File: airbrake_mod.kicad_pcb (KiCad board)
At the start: 2 copper layers, 107.9 x 107.9 mm, 78 parts, among them J1 Conn_Coaxial, J2 USB_C_Receptacle_USB2.0_16P, J3 Conn_01x06_Socket, SW4 SW_Push_Shielded, SW5 SW_Push_Shielded, SW6 SW_Push_Shielded, SW7 SW_Push_Shielded, U1 STM32H743VITx, U2 MAX-M8C, U3 TPS54560BDDA, U4 AP7361C-33E, U5 AP7361C-33E, U6 MX25L25645GM2I, U7 DSF105Q9R0HDR

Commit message: Power Supply Speccing, IMU, Eyeballs
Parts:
- added C23: 4.7u, Capacitor_SMD:C_0805_2012Metric, F.Cu at (105.4, 52.4)
- added U8: LSM6DSO32, Package_LGA:LGA-14_3x2.5mm_P0.5mm_LayoutBorder3x4y, F.Cu at (106.0, 55.0)
- C14, C3, C4, C5, C6, C7: value C -> 4.7u
- C15, C16, C20, C21: value C -> 47u
- C17: value C -> 0.1u
- D1, D2: value LED_Filled -> QBLP601-R5-2897
- L1: value L -> 22u
- R10: value R_US -> 18k
- R12: value R_US -> 82k
- R15, R16: value R_US -> 240
- R17, R18, R19, R20: value R_US -> 5k
- R7, R8: value R_US -> 300k
- R9: value R_US -> 62k
- moved BZ1 5.04 mm to (144.8, 91.9), turned to 90 degrees
- moved C7 0.08 mm to (57.0, 72.7)
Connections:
- U1 pad 32: unconnected-(U1-PC4-Pad32) -> ACCEL_CS
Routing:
- net 3V3_Sensors: track 67.4 -> 131.8 mm, vias 0 -> 2
- net 3V3_MCU: track 170.2 -> 183.2 mm
- net Buzzer_H: track 69.9 -> 79.6 mm
- net ACCEL_CS: track 0.00 -> 8.76 mm
- net MODE_3: track 8.68 -> 17.2 mm
- net MODE_2: track 9.47 -> 17.3 mm
- net MODE_1: track 10.0 -> 17.6 mm
- net MODE_0: track 13.2 -> 20.3 mm
- net ACCEL_SDI: track 2.98 -> 9.74 mm
- net ACCEL_SDO: track 3.59 -> 9.97 mm
- net MCU_I2C1_SCL: track 45.6 -> 40.3 mm
- net ACCEL_SCLK: track 3.48 -> 8.35 mm, vias 0 -> 2
- net Buzzer_L: track 68.2 -> 72.9 mm
- net FLASH_SPI_SCLK: track 43.2 -> 45.0 mm
- net -BATT: track 87.9 -> 88.9 mm, vias 72 -> 75

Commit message: Release Candidate 1
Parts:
- removed the G*** at (63.4, 230.4)
- added C24: 4.7u, Capacitor_SMD:C_0805_2012Metric, F.Cu at (146.2, 80.4)
- added C25: 4.7u, Capacitor_SMD:C_0805_2012Metric, F.Cu at (52.0, 105.5)
- added D6: CLV1L-FKB, LED_SMD:LED_Cree-PLCC4_3.2x2.8mm_CCW, F.Cu at (95.3, 48.3)
- added D7: QBLP601-R5-2897, LED_SMD:LED_0603_1608Metric, F.Cu at (117.8, 51.1)
- added D8: QBLP601-R5-2897, LED_SMD:LED_0603_1608Metric, F.Cu at (103.2, 58.3)
- added D9: CLV1L-FKB, LED_SMD:LED_Cree-PLCC4_3.2x2.8mm_CCW, F.Cu at (121.5, 54.0)
- added J4: Conn_01x03_Socket, Connector_Molex:Molex_Micro-Fit_3.0_43650-0315_1x03_P3.00mm_Vertical, F.Cu at (146.2, 91.2)
- added J5: Conn_01x03_Socket, Connector_JST:JST_XH_B3B-XH-A_1x03_P2.50mm_Vertical, F.Cu at (118.3, 146.4)
- added J6: Conn_02x02_Counter_Clockwise, Connector_PinHeader_1.00mm:PinHeader_2x02_P1.00mm_Vertical, F.Cu at (140.8, 83.1)
- added Q1: DMG2302U, Package_TO_SOT_SMD:SOT-23, F.Cu at (138.0, 89.2)
- added Q2: Si2319CDS, Package_TO_SOT_SMD:SOT-23, F.Cu at (141.4, 89.2)
- added Q3: DMG2302U, Package_TO_SOT_SMD:SOT-23, F.Cu at (140.0, 104.9)
- added Q4: Si2319CDS, Package_TO_SOT_SMD:SOT-23, F.Cu at (141.5, 69.8)
- added Q5: Si2319CDS, Package_TO_SOT_SMD:SOT-23, F.Cu at (138.0, 69.8)
- added R23: 43, Resistor_SMD:R_0805_2012Metric, F.Cu at (94.1, 51.8)
- added R24: 43, Resistor_SMD:R_0805_2012Metric, F.Cu at (95.4, 55.2)
- added R25: 110, Resistor_SMD:R_0805_2012Metric, F.Cu at (96.2, 51.8)
- added R26: 240, Resistor_SMD:R_0805_2012Metric, F.Cu at (111.4, 57.0)
- added R27: 240, Resistor_SMD:R_0805_2012Metric, F.Cu at (99.7, 60.2)
- added R29: 110, Resistor_SMD:R_0805_2012Metric, F.Cu at (117.5, 55.3)
- added R30: 43, Resistor_SMD:R_0805_2012Metric, F.Cu at (117.5, 59.1)
- added R31: 43, Resistor_SMD:R_0805_2012Metric, F.Cu at (117.5, 57.2)
- added R32: 56k, Resistor_SMD:R_0805_2012Metric, F.Cu at (137.4, 64.0)
- added R33: 100k, Resistor_SMD:R_0805_2012Metric, F.Cu at (113.5, 62.4)
- added R34: 100k, Resistor_SMD:R_0805_2012Metric, F.Cu at (113.5, 65.8)
- added SW1: SW_Push_Shielded, 0_airbrake_footprints:R-667766, F.Cu at (107.6, 61.4)
- added SW2: SW_Push_Shielded, 0_airbrake_footprints:R-667766, F.Cu at (138.2, 96.2)
- added SW3: SW_Rotary_1x4_MP, 0_airbrake_footprints:S-2051, F.Cu at (54.6, 112.2)
- added SW9: SW_SPDT_321, 0_airbrake_footprints:CL-SB-12A-01T, F.Cu at (147.9, 100.0)
- added U10: BD4860G-TR, Package_TO_SOT_SMD:SOT-23-5, F.Cu at (131.2, 59.2)
- added U9: BME680, Package_LGA:Bosch_LGA-8_3x3mm_P0.8mm_ClockwisePinNumbering, F.Cu at (61.8, 106.3)
- added Y1: Crystal_GND24, Crystal:Crystal_SMD_2016-4Pin_2.0x1.6mm, F.Cu at (110.3, 71.0)
- BZ1: footprint Buzzer_Beeper:Buzzer_TDK_PS1240P02BT_D12.2mm_H6.5mm -> 0_airbrake_footprints:CMT-322-65-SMT-TR
- C1, C2: value C -> 8p
- moved BZ1 17.7 mm to (140.0, 108.9), turned to 180 degrees
- moved D4 17.0 mm to (138.6, 114.4)
- moved R21 14.9 mm to (137.4, 120.5), turned to -90 degrees
- moved R22 11.4 mm to (138.0, 117.6), turned to 0 degrees
- moved D5 3.61 mm to (137.4, 128.6), turned to 90 degrees
- moved C22 0.64 mm to (140.5, 74.2), turned to 180 degrees
- moved C2 0.62 mm to (112.3, 69.0), turned to -45 degrees
- moved C1 0.58 mm to (112.3, 72.9), turned to -135 degrees
- moved C6 0.21 mm to (109.5, 77.3)
- moved R19 0.15 mm to (109.2, 81.5)
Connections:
- net MCU_I2C1_SCL renamed EXT_I2C1_SCL
- net MCU_I2C1_SDA renamed EXT_I2C1_SDA
- net MCU_I2C3_SCL renamed BME680_I2C3_SCL
- net MCU_I2C3_SDA renamed BME680_I2C3_SDA
- BZ1 pad 1: Buzzer_H -> 3V6_SWITCHING
- BZ1 pad 2: Buzzer_L -> Net-(BZ1--)
- D4 pad 2: +BATT -> +BATT_SW
- U1 pad 15: MODE_0 -> STATUS1_R
- U1 pad 16: MODE_1 -> STATUS1_G
- U1 pad 17: MODE_2 -> STATUS1_B
- U1 pad 18: MODE_3 -> unconnected-(U1-PC3_C-Pad18)
- U1 pad 34: unconnected-(U1-PB0-Pad34) -> STATUS1
- U1 pad 35: unconnected-(U1-PB1-Pad35) -> STATUS_POW
- U1 pad 38: Buzzer_L -> unconnected-(U1-PE8-Pad38)
- U1 pad 40: unconnected-(U1-PE10-Pad40) -> BAT_OK_MCU
- U1 pad 41: unconnected-(U1-PE11-Pad41) -> STATUS0_R
- U1 pad 43: unconnected-(U1-PE13-Pad43) -> STATUS0_G
- U1 pad 44: unconnected-(U1-PE14-Pad44) -> STATUS0_B
- U1 pad 47: unconnected-(U1-PB11-Pad47) -> GPS_TP
- U1 pad 51: unconnected-(U1-PB12-Pad51) -> VBUS_DETECT
- U1 pad 81: unconnected-(U1-PD0-Pad81) -> MODE_0
- U1 pad 82: unconnected-(U1-PD1-Pad82) -> MODE_1
- U1 pad 83: unconnected-(U1-PD2-Pad83) -> MODE_2
- U1 pad 84: unconnected-(U1-PD3-Pad84) -> MODE_3
- U1 pad 91: unconnected-(U1-PB5-Pad91) -> SERVO_EN
- U1 pad 95: unconnected-(U1-PB8-Pad95) -> SERVO_SIG
- U2 pad 4: unconnected-(U2-TIMEPULSE-Pad4) -> GPS_TP
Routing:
- net 3V6_SWITCHING: track 9.08 -> 220.0 mm, vias 0 -> 8
- net +BATT: track 1.77 -> 137.1 mm, vias 10 -> 0
- net BAT_OK: track 0.00 -> 81.7 mm, vias 0 -> 4
- net Buzzer_L: track 72.9 -> 0.00 mm, vias 2 -> 0
- net Net-(Q4-G): track 0.00 -> 61.6 mm, vias 0 -> 5
- net MODE_3: track 17.2 -> 76.1 mm
- net 3V3_MCU: track 183.2 -> 239.8 mm, vias 4 -> 8
- net MODE_2: track 17.3 -> 72.3 mm
- net SERVO_SIG: track 0.00 -> 54.3 mm, vias 0 -> 2
- net MODE_1: track 17.6 -> 68.1 mm
- net GPS_TP: track 0.00 -> 46.0 mm, vias 0 -> 4
- net SERVO_EN: track 0.00 -> 45.5 mm, vias 0 -> 2
- net Net-(U1-BOOT0): track 2.46 -> 47.0 mm, vias 0 -> 2
- net MODE_0: track 20.3 -> 61.9 mm, vias 2 -> 0
- net -BATT: track 88.9 -> 120.2 mm, vias 75 -> 83
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- removed copper zone on B.Cu, net +BATT
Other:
- board text added: "+"
- board text added: "BOOT"
- board text added: "Clarkson University Rocketry 2025 Airbrakes Module"
- board text added: "RST"
- board text removed: "Clarkson University Rocketry Lithobrake Module"
- board text removed: "Needs Zip Tie holes to allow for battery swap"
- board text removed: "Yes, there is a huge current loop because of the batteries. No, there isn't anything that matters. Not even the GPS."

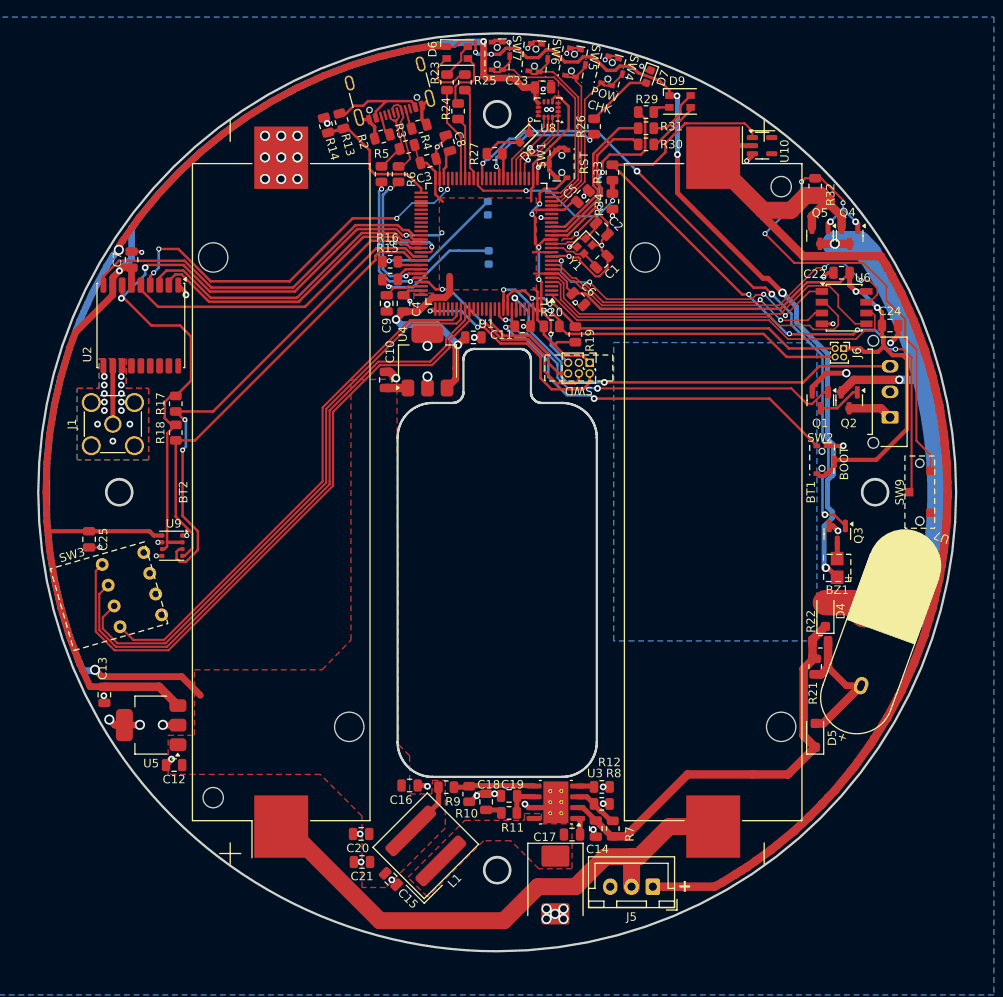
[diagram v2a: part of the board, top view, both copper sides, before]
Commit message: Release Candidate 2
Incorporates fixes for all identified issues in the PCBR
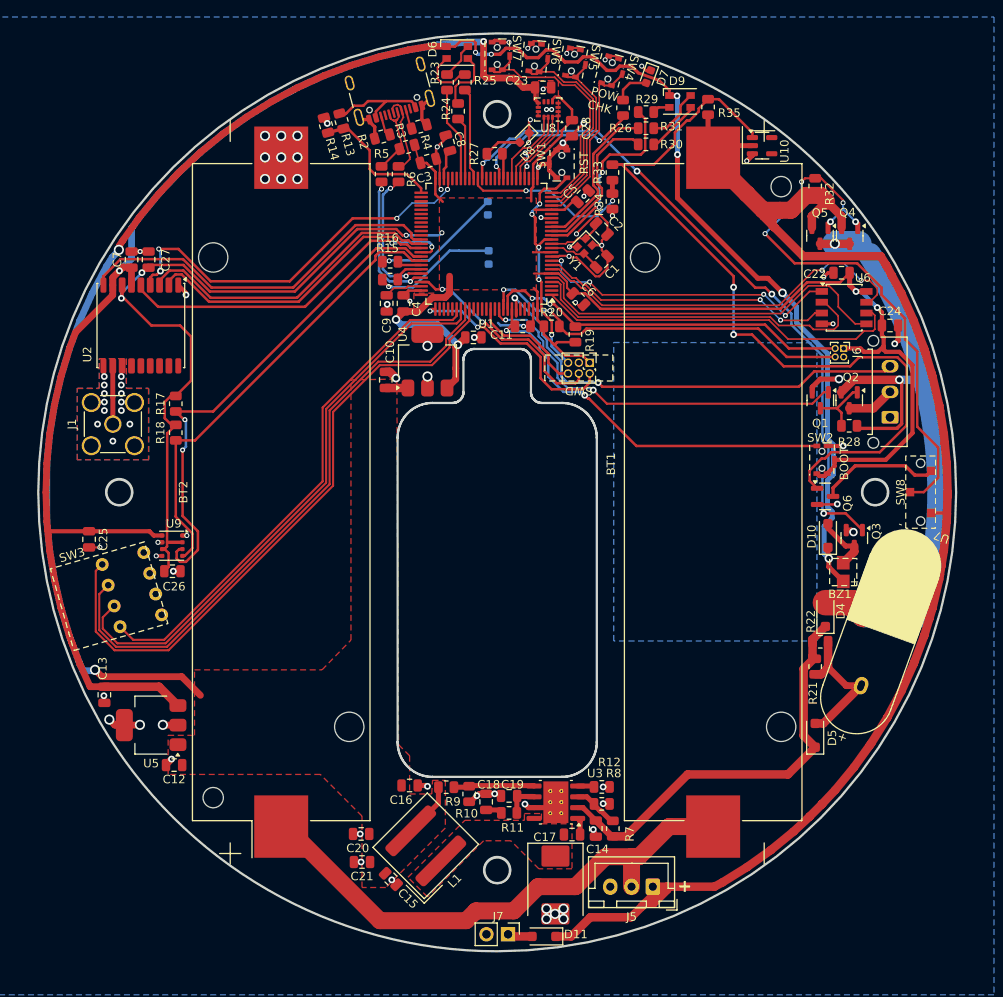
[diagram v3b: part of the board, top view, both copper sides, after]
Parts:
- removed SW9: SW_SPDT_321, 0_airbrake_footprints:CL-SB-12A-01T
- added C26: 4.7u, Capacitor_SMD:C_0805_2012Metric, F.Cu at (61.8, 109.3)
- added C27: 4.7u, Capacitor_SMD:C_0805_2012Metric, F.Cu at (59.0, 72.7)
- added C28: 4.7u, Capacitor_SMD:C_0805_2012Metric, F.Cu at (108.8, 57.2)
- added D10: NRVB120VLSFT1G, Diode_SMD:D_SOD-123F, F.Cu at (138.9, 105.1)
- added D11: NRVB120VLSFT1G, Diode_SMD:D_SOD-123F, F.Cu at (105.5, 152.2)
- added J7: Conn_01x02_Pin, Connector_PinHeader_2.54mm:PinHeader_1x02_P2.54mm_Vertical, F.Cu at (101.3, 152.0)
- added Q6: DMG2302U, Package_TO_SOT_SMD:SOT-23, F.Cu at (138.6, 100.5)
- added R28: 10k, Resistor_SMD:R_0805_2012Metric, F.Cu at (141.4, 92.2)
- added R35: 100k, Resistor_SMD:R_0805_2012Metric, F.Cu at (124.8, 54.7)
- added SW8: SW_SPDT_321, 0_airbrake_footprints:CL-SB-12A-01T, F.Cu at (148.1, 100.0)
- R32: value 56k -> 220k
- U10: value BD4860G-TR -> BD4960G-TR
- moved R26 4.05 mm to (114.8, 54.8)
- moved Q3 2.06 mm to (142.0, 105.4)
- moved BZ1 0.86 mm to (140.7, 109.4)
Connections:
- net BAT_OK renamed Net-(Q6-G)
- net GPS_TP renamed GPS_TIME
- net STATUS1 renamed STATUS2
- BT2 pad 2: -BATT -> GND
- C1 pad 1: -BATT -> GND
- C10 pad 2: -BATT -> GND
- C11 pad 2: -BATT -> GND
- C12 pad 2: -BATT -> GND
- C13 pad 2: -BATT -> GND
- C14 pad 2: -BATT -> GND
- C15 pad 2: -BATT -> GND
- C16 pad 2: -BATT -> GND
- C18 pad 2: -BATT -> GND
- C19 pad 2: -BATT -> GND
- C2 pad 2: -BATT -> GND
- C20 pad 2: -BATT -> GND
- C21 pad 2: -BATT -> GND
- C22 pad 2: -BATT -> GND
- C23 pad 2: -BATT -> GND
- C24 pad 2: -BATT -> GND
- C25 pad 2: -BATT -> GND
- C3 pad 2: -BATT -> GND
- C4 pad 2: -BATT -> GND
- C5 pad 2: -BATT -> GND
- C6 pad 2: -BATT -> GND
- C7 pad 2: -BATT -> GND
- C8 pad 1: -BATT -> GND
- C9 pad 1: -BATT -> GND
- D1 pad 1: -BATT -> GND
- D2 pad 1: -BATT -> GND
- D3 pad 2: -BATT -> GND
- D7 pad 1: -BATT -> GND
- D8 pad 1: -BATT -> GND
- J1 pad 2: -BATT -> GND
- J2 pad A1: -BATT -> GND
- J2 pad A12: -BATT -> GND
- J2 pad B1: -BATT -> GND
- J2 pad B12: -BATT -> GND
- J2 pad S1: -BATT -> GND
- J3 pad 3: -BATT -> GND
- J4 pad 1: SERVO+ -> GND
- J4 pad 2: SERVO_POW -> SERVO+
- J5 pad 3: -BATT -> GND
- J6 pad 2: -BATT -> GND
- Q1 pad 2: -BATT -> GND
- Q3 pad 2: -BATT -> GND
- R1 pad 1: -BATT -> GND
- R10 pad 2: -BATT -> GND
- R12 pad 2: -BATT -> GND
- R14 pad 2: -BATT -> GND
- R2 pad 2: -BATT -> GND
- R3 pad 2: -BATT -> GND
- R34 pad 2: -BATT -> GND
- R8 pad 2: -BATT -> GND
- SW1 pad 2: -BATT -> GND
- SW1 pad SH: -BATT -> GND
- SW2 pad SH: -BATT -> GND
- SW3 pad 5: -BATT -> GND
- SW4 pad 1: -BATT -> GND
- SW4 pad SH: -BATT -> GND
- SW5 pad 1: -BATT -> GND
- SW5 pad SH: -BATT -> GND
- SW6 pad 1: -BATT -> GND
- SW6 pad SH: -BATT -> GND
- SW7 pad 1: -BATT -> GND
- SW7 pad SH: -BATT -> GND
- U1 pad 10: -BATT -> GND
- U1 pad 19: -BATT -> GND
- U1 pad 26: -BATT -> GND
- U1 pad 49: -BATT -> GND
- U1 pad 74: -BATT -> GND
- U1 pad 99: -BATT -> GND
- U10 pad 3: -BATT -> GND
- U2 pad 1: -BATT -> GND
- U2 pad 10: -BATT -> GND
- U2 pad 12: -BATT -> GND
- U3 pad 7: -BATT -> GND
- U3 pad 9: -BATT -> GND
- U4 pad 2: -BATT -> GND
- U5 pad 2: -BATT -> GND
- U6 pad 4: -BATT -> GND
- U7 pad 2: -BATT -> GND
- U8 pad 2: -BATT -> GND
- U8 pad 3: -BATT -> GND
- U8 pad 6: -BATT -> GND
- U8 pad 7: -BATT -> GND
- U9 pad 1: -BATT -> GND
- U9 pad 5: -BATT -> GND
- U9 pad 7: -BATT -> GND
- Y1 pad 2: -BATT -> GND
- Y1 pad 4: -BATT -> GND
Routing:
- net GND: track 0.00 -> 129.2 mm, vias 0 -> 88
- net -BATT: track 120.2 -> 0.00 mm, vias 83 -> 0
- net +BATT: track 137.1 -> 165.5 mm
- net Net-(Q6-D): track 0.00 -> 14.3 mm
- net Net-(Q6-G): track 81.7 -> 95.2 mm, vias 4 -> 2
- net +BATT_SW: track 29.8 -> 38.9 mm
- net Net-(BZ1--): track 1.97 -> 7.02 mm
- net 3V3_MCU: track 239.8 -> 244.7 mm
- net Net-(Q4-G): track 61.6 -> 66.3 mm
- net STATUS_POW: track 15.9 -> 20.3 mm
- net Net-(D7-A): track 7.86 -> 4.25 mm
- net Net-(D11-A): track 0.00 -> 2.93 mm
- net BUTT_3: track 26.3 -> 28.6 mm
- net BUTT_2: track 22.9 -> 25.3 mm
- net 3V6_SWITCHING: track 220.0 -> 222.3 mm
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- added copper zone on B.Cu, net GND
- added copper zone on F.Cu, net GND
- removed copper zone on B.Cu, net -BATT
- removed copper zone on F.Cu, net -BATT

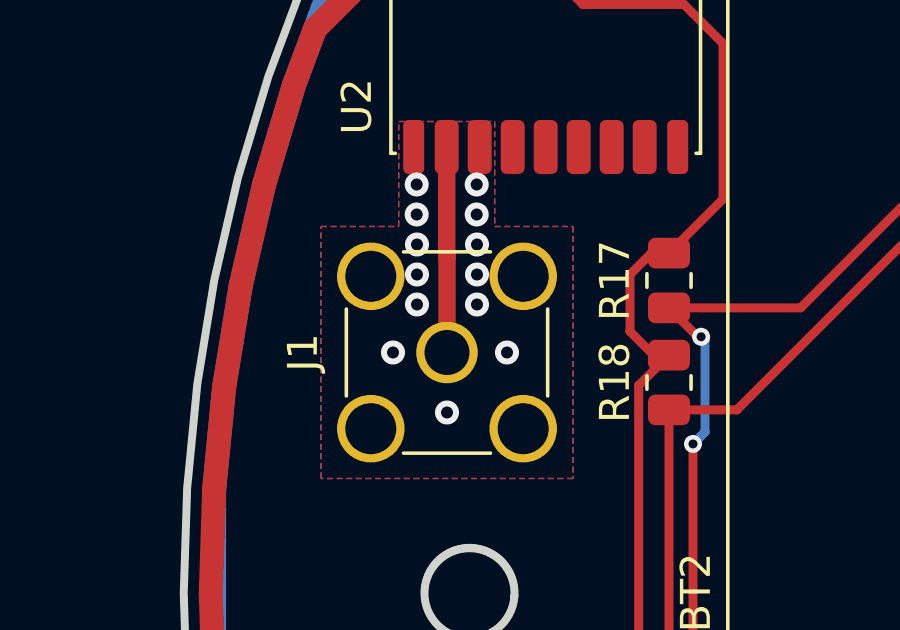
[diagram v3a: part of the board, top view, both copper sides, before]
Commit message: Release Candidate 3
Fixed name, one location with vias. Added production files in prep for merge request.
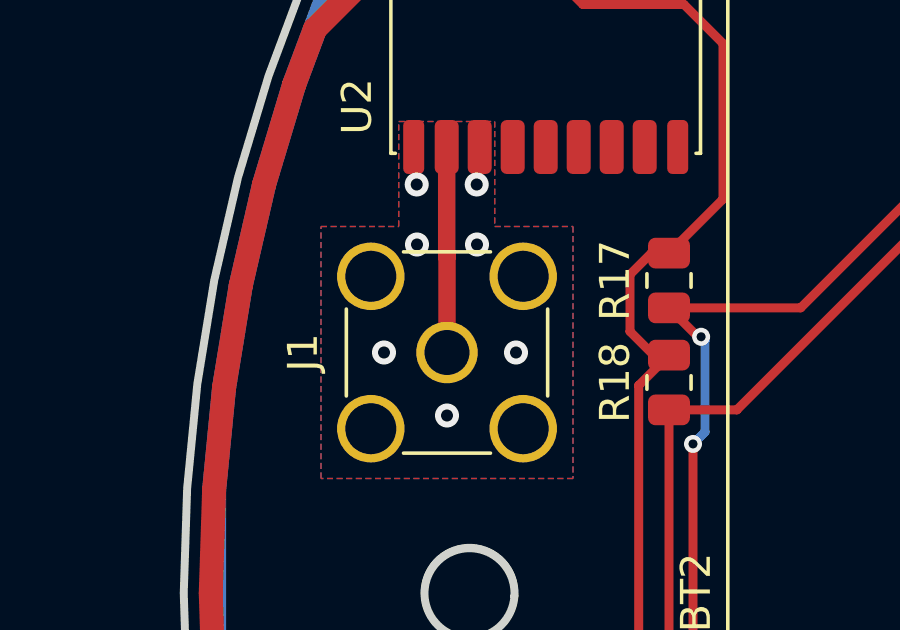
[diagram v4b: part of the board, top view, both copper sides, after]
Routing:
- net GND: vias 88 -> 82
